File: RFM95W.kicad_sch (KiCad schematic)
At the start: 3 parts, among them U1 RFM95W-915S2

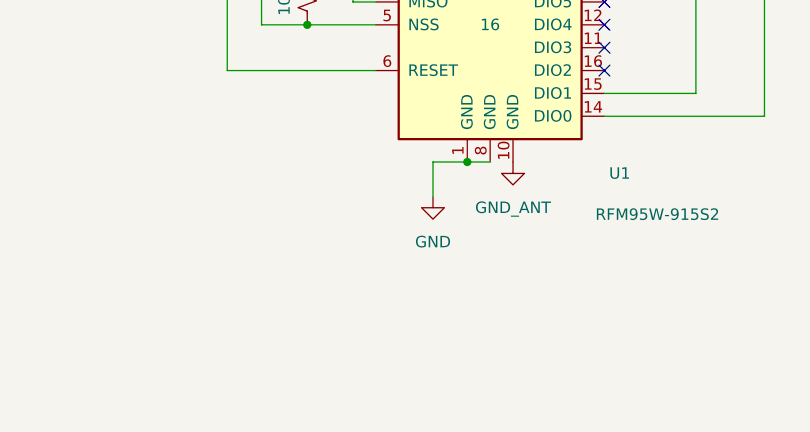
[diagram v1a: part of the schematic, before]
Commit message: cleanup. ERC and DRC good. No footprint yet.
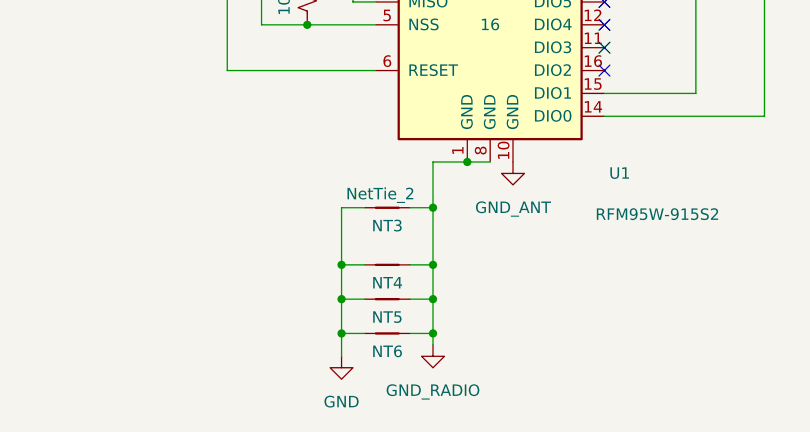
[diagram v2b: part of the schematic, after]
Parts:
- added NT3, NT4, NT5, NT6: NetTie_2, ProjectLib:NetTie-2_SMD_Pad0.5mm, symbol ProjectLib:NetTie_2
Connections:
- net GND: now also NT3.1, NT4.1, NT5.1, NT6.1; no longer U1.1 (GND), U1.8 (GND)
- new net GND_RADIO: NT3.2, NT4.2, NT5.2, NT6.2, U1.1 (GND), U1.8 (GND)

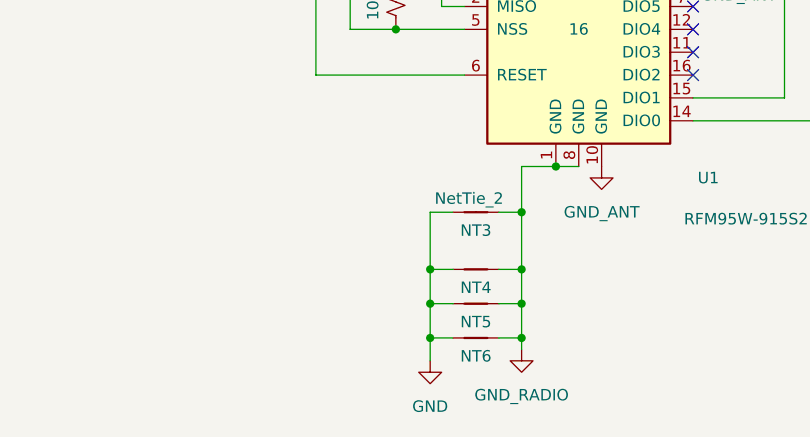
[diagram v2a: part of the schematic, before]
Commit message: added footprint and step model. Cleaned up silkscreen and fab layers.
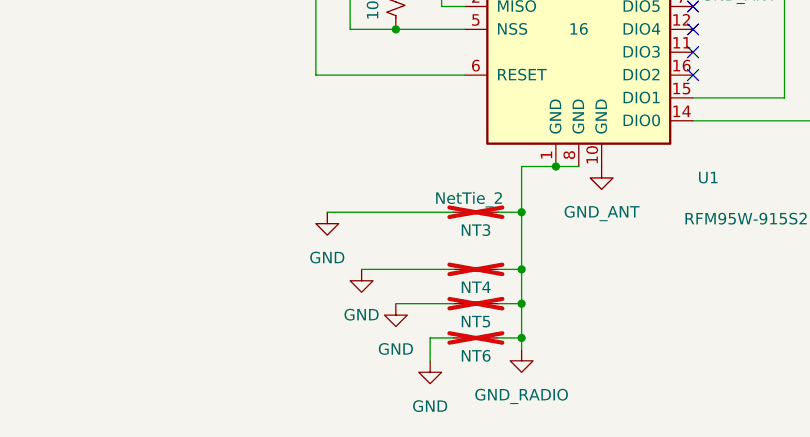
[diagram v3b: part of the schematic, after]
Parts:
- NT3, NT4, NT5, NT6: now not fitted
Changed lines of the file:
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@@
-	)
-	(junction
-		(at 99.06 119.38)
-		(diameter 0)
-		(color 0 0 0 0)
-	)
-	(junction
-		(at 99.06 111.76)
-		(diameter 0)
-		(color 0 0 0 0)
-	)
-	(junction
-		(at 99.06 115.57)
-		(diameter 0)
-		(color 0 0 0 0)
 	)
 	(junction
@@
 	(wire
 		(pts
+			(xy 91.44 111.76) (xy 101.6 111.76)
+		)
+		(stroke
+			(width 0)
+			(type default)
+		)
+	)
+	(wire
+		(pts
 			(xy 109.22 119.38) (xy 109.22 120.65)
 		)
@@
 	(wire
 		(pts
-			(xy 99.06 105.41) (xy 99.06 111.76)
-		)
-		(stroke
-			(width 0)
-			(type default)
-		)
-	)
-	(wire
-		(pts
 			(xy 152.4 53.34) (xy 154.94 55.88)
 		)
@@
 	(wire
 		(pts
+			(xy 87.63 105.41) (xy 101.6 105.41)
+		)
+		(stroke
+			(width 0)
+			(type default)
+		)
+	)
+	(wire
+		(pts
 			(xy 109.22 105.41) (xy 109.22 111.76)
 		)
@@
 	(wire
 		(pts
-			(xy 99.06 115.57) (xy 101.6 115.57)
-		)
-		(stroke
-			(width 0)
-			(type default)
-		)
-	)
-	(wire
-		(pts
 			(xy 109.22 111.76) (xy 109.22 115.57)
 		)
@@
 	(wire
 		(pts
-			(xy 99.06 111.76) (xy 99.06 115.57)
-		)
-		(stroke
-			(width 0)
-			(type default)
-		)
-	)
-	(wire
-		(pts
 			(xy 138.43 73.66) (xy 138.43 92.71)
 		)
@@
 	(wire
 		(pts
+			(xy 95.25 115.57) (xy 101.6 115.57)
+		)
+		(stroke
+			(width 0)
+			(type default)
+		)
+	)
+	(wire
+		(pts
 			(xy 128.27 95.25) (xy 146.05 95.25)
 		)
@@
 	(wire
 		(pts
-			(xy 99.06 115.57) (xy 99.06 119.38)
-		)
-		(stroke
-			(width 0)
-			(type default)
-		)
-	)
-	(wire
-		(pts
 			(xy 90.17 85.09) (xy 95.25 85.09)
 		)
@@
 		)
 	)
-	(wire
-		(pts
-			(xy 99.06 111.76) (xy 101.6 111.76)
-		)
-		(stroke
-			(width 0)
-			(type default)
-		)
-	)
 	(bus
 		(pts
 			(xy 154.94 63.5) (xy 154.94 76.2)
-		)
-		(stroke
-			(width 0)
-			(type default)
-		)
-	)
-	(wire
-		(pts
-			(xy 101.6 105.41) (xy 99.06 105.41)
 		)
 		(stroke
@@
 	(symbol
 		(lib_id "power:GND")
+		(at 87.63 105.41 0)
+		(unit 1)
+		(exclude_from_sim no)
+		(in_bom yes)
+		(on_board yes)
+		(dnp no)
+		(fields_autoplaced yes)
+		(property "Reference" "#PWR029"
+			(at 87.63 111.76 0)
+			(effects
+				(font
+					(size 1.27 1.27)
+				)
+				(hide yes)
+			)
+		)
+		(property "Value" "GND"
+			(at 87.63 110.49 0)
+			(effects
+				(font
+					(size 1.27 1.27)
+				)
+			)
+		)
+		(property "Footprint" ""
+			(at 87.63 105.41 0)
+			(effects
+				(font
+					(size 1.27 1.27)
+				)
+				(hide yes)
+			)
+		)
+		(property "Datasheet" ""
+			(at 87.63 105.41 0)
+			(effects
+				(font
+					(size 1.27 1.27)
+				)
+				(hide yes)
+			)
+		)
+		(property "Description" "Power symbol creates a global label with name \"GND\" , ground"
+			(at 87.63 105.41 0)
+			(effects
+				(font
+					(size 1.27 1.27)
+				)
+				(hide yes)
+			)
+		)
+		(pin "1"
+		)
+		(instances
+			(project ""
+				(path "/0c2d0c14-8850-4a30-bb78-b2f40cb442ba/2db29b35-1005-45eb-b852-0b853354466f"
+					(reference "#PWR029")
+					(unit 1)
+				)
+			)
+		)
+	)
+	(symbol
+		(lib_id "power:GND")
 		(at 99.06 121.92 0)
 		(unit 1)
@@
 		(in_bom no)
 		(on_board yes)
-		(dnp no)
+		(dnp yes)
 		(property "Reference" "NT3"
 			(at 104.14 107.442 0)
@@
 				(path "/0c2d0c14-8850-4a30-bb78-b2f40cb442ba/2db29b35-1005-45eb-b852-0b853354466f"
 					(reference "NT3")
+					(unit 1)
+				)
+			)
+		)
+	)
+	(symbol
+		(lib_id "power:GND")
+		(at 95.25 115.57 0)
+		(unit 1)
+		(exclude_from_sim no)
+		(in_bom yes)
+		(on_board yes)
+		(dnp no)
+		(fields_autoplaced yes)
+		(property "Reference" "#PWR027"
+			(at 95.25 121.92 0)
+			(effects
+				(font
+					(size 1.27 1.27)
+				)
+				(hide yes)
+			)
+		)
+		(property "Value" "GND"
+			(at 95.25 120.65 0)
+			(effects
+				(font
+					(size 1.27 1.27)
+				)
+			)
+		)
+		(property "Footprint" ""
+			(at 95.25 115.57 0)
+			(effects
+				(font
+					(size 1.27 1.27)
+				)
+				(hide yes)
+			)
+		)
+		(property "Datasheet" ""
+			(at 95.25 115.57 0)
+			(effects
+				(font
+					(size 1.27 1.27)
+				)
+				(hide yes)
+			)
+		)
+		(property "Description" "Power symbol creates a global label with name \"GND\" , ground"
+			(at 95.25 115.57 0)
+			(effects
+				(font
+					(size 1.27 1.27)
+				)
+				(hide yes)
+			)
+		)
+		(pin "1"
+		)
+		(instances
+			(project ""
+				(path "/0c2d0c14-8850-4a30-bb78-b2f40cb442ba/2db29b35-1005-45eb-b852-0b853354466f"
+					(reference "#PWR027")
 					(unit 1)
 				)
@@
 		(in_bom no)
 		(on_board yes)
-		(dnp no)
+		(dnp yes)
 		(property "Reference" "NT5"
 			(at 104.14 117.602 0)
@@
 		(in_bom no)
 		(on_board yes)
-		(dnp no)
+		(dnp yes)
 		(property "Reference" "NT4"
 			(at 104.14 113.792 0)
@@
 		(in_bom no)
 		(on_board yes)
-		(dnp no)
+		(dnp yes)
 		(property "Reference" "NT6"
 			(at 104.14 121.412 0)
@@
 					(unit 1)
 				)
+			)
+		)
+	)
+	(symbol
+		(lib_id "power:GND")
+		(at 91.44 111.76 0)
+		(unit 1)
+		(exclude_from_sim no)
+		(in_bom yes)
+		(on_board yes)
+		(dnp no)
+		(fields_autoplaced yes)
+		(property "Reference" "#PWR028"
+			(at 91.44 118.11 0)
+			(effects
+				(font
+					(size 1.27 1.27)
+				)
+				(hide yes)
+			)
+		)
+		(property "Value" "GND"
+			(at 91.44 116.84 0)
+			(effects
+				(font
+					(size 1.27 1.27)
+				)
+			)
+		)
+		(property "Footprint" ""
+			(at 91.44 111.76 0)
+			(effects
+				(font
+					(size 1.27 1.27)
+				)
+				(hide yes)
+			)
+		)
+		(property "Datasheet" ""
+			(at 91.44 111.76 0)
+			(effects
+				(font
+					(size 1.27 1.27)
+				)
+				(hide yes)
+			)
+		)
+		(property "Description" "Power symbol creates a global label with name \"GND\" , ground"
+			(at 91.44 111.76 0)
+			(effects
+				(font
+					(size 1.27 1.27)
+				)
+				(hide yes)
+			)
+		)
+		(pin "1"
+		)
+		(instances
+			(project ""
+				(path "/0c2d0c14-8850-4a30-bb78-b2f40cb442ba/2db29b35-1005-45eb-b852-0b853354466f"
+					(reference "#PWR028")
+					(unit 1)
+				)
